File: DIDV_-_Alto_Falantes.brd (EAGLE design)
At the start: 74.9 x 59.4 mm, 41 parts, among them J101 PG203J, J102 PG203J, U101 LM386M, U102 LM386M

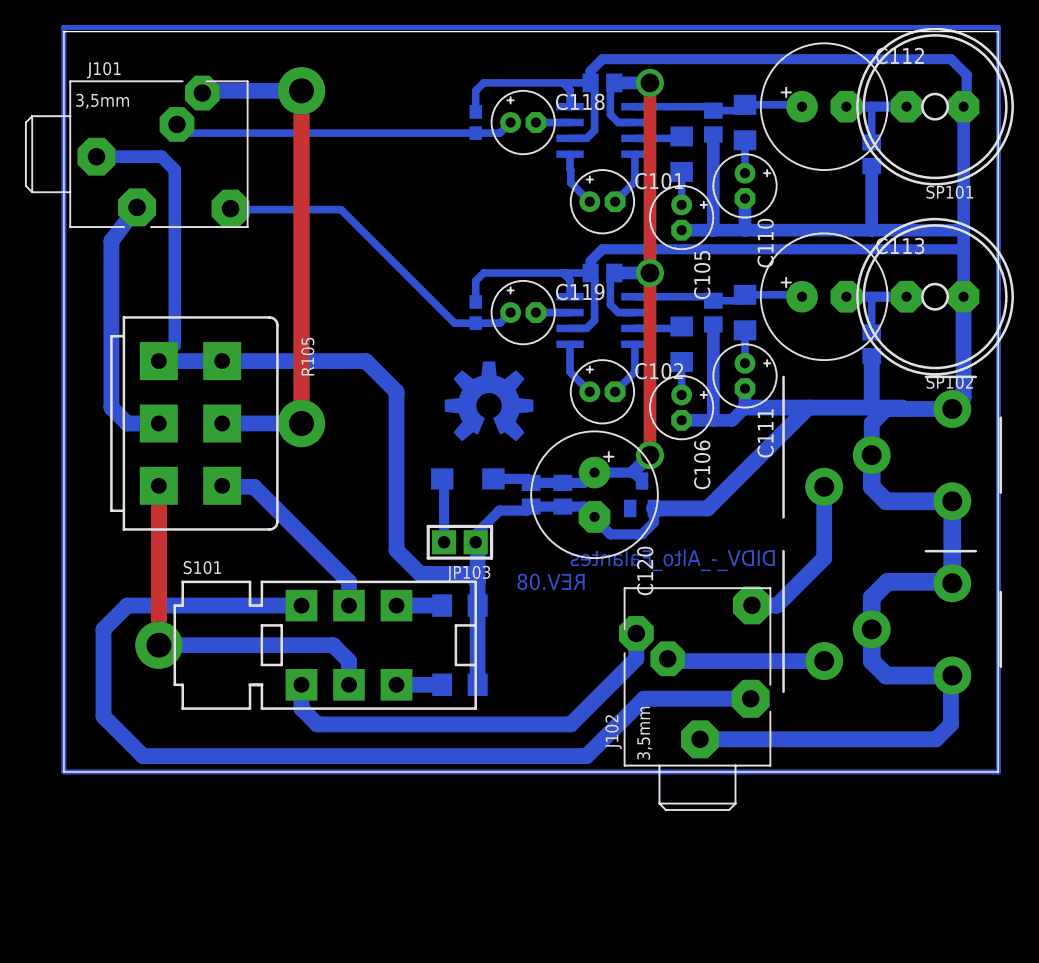
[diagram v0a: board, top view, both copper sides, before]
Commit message: Revisão 9
- Corrigidos algumas falhas de ligação
- Implementação com VPRG dos TLCs via Hardware
- Inserção do cálculo do Riref

Obs. Se somente a criação de boards, não será incrementado. No caso, se criado um board novo board vou subir para 9.1 e assim por diante.
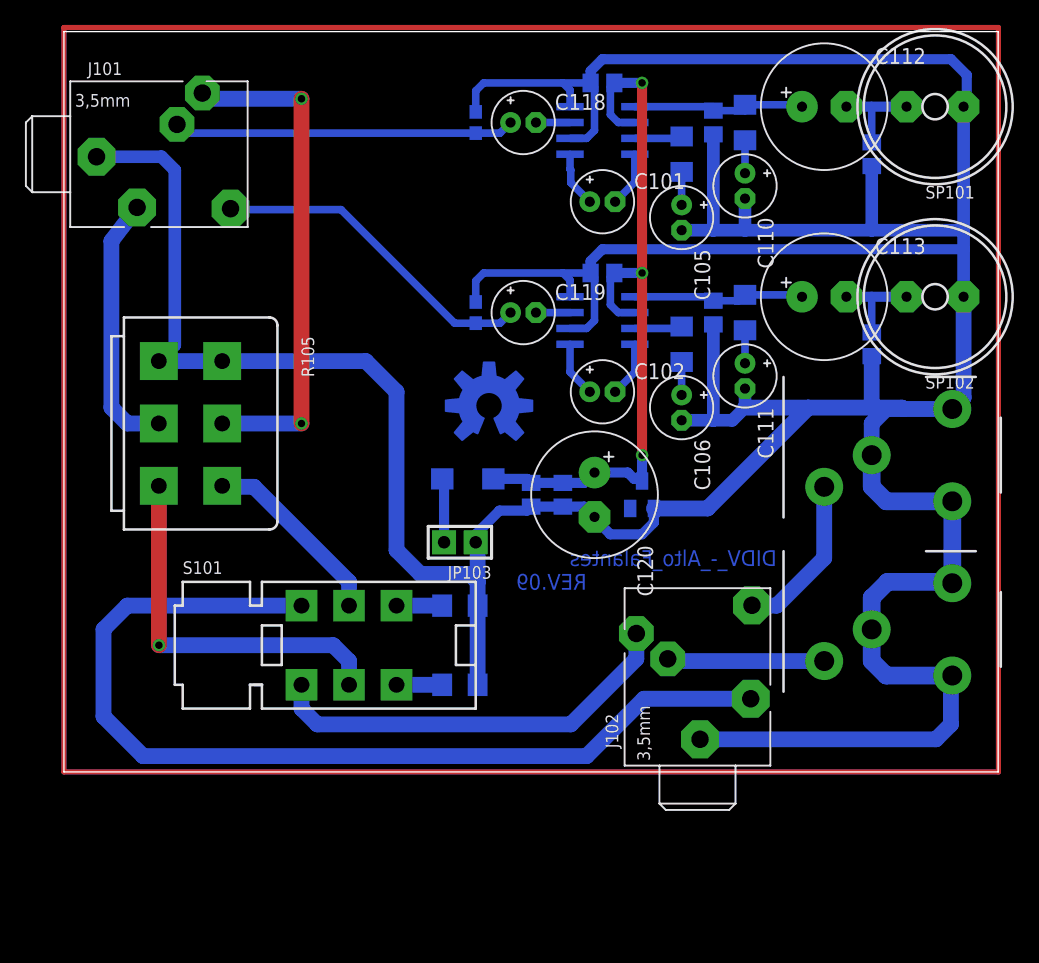
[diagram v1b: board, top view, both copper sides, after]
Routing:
- net N$20: track 0.00 -> 269.2 mm
- net VCC: track 60.0 -> 58.8 mm
- net A_R: track 41.9 -> 41.0 mm
- added copper zone on layer 1, net N$22
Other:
- board text added: "REV.09"
- board text removed: "REV.08"

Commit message: Revisão 10
Revisão representa o estado final do projeto, alterações agora somente referentes a valores de componentes e adaptações se e somente se não existir a possibilidade de manobras via software.

Placas nas dimensões e condições as quais foram submetidas a cotação para confecção em local especializado.
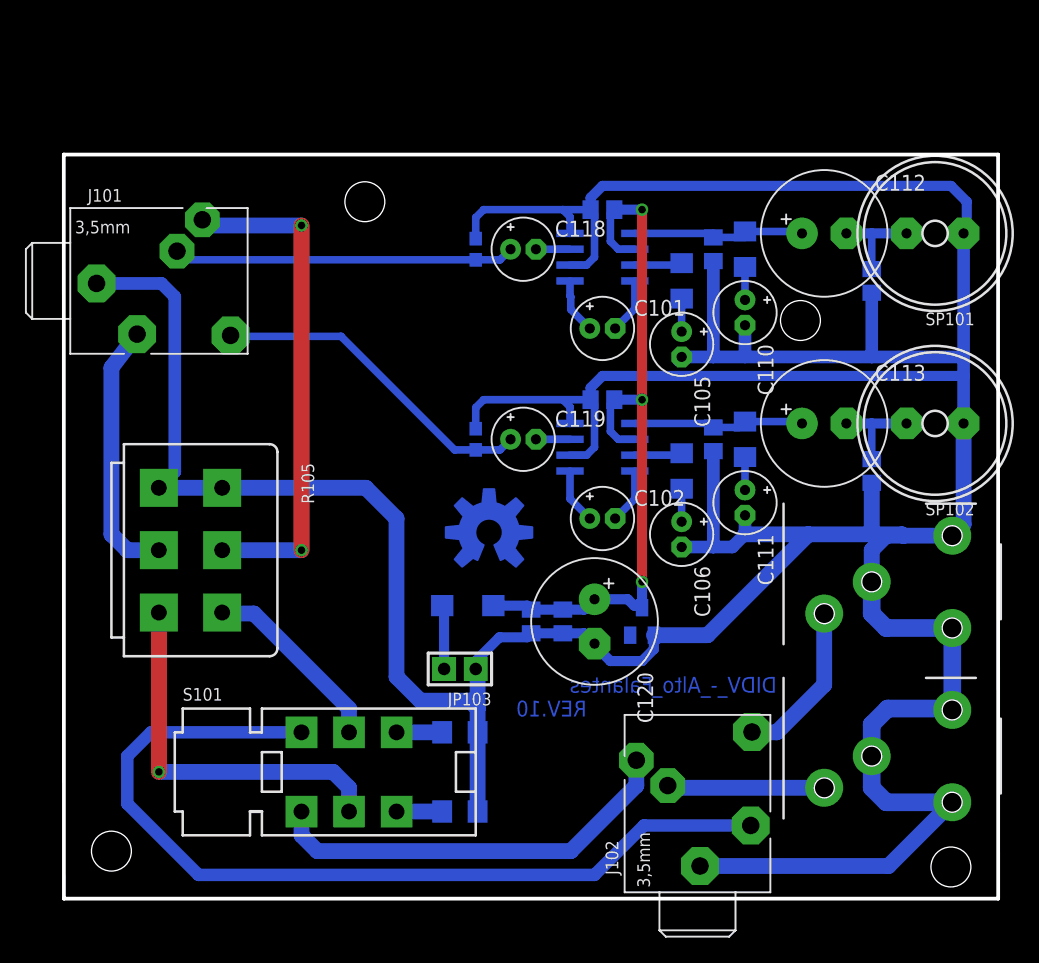
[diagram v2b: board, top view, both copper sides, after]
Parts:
- moved C101 10.2 mm to (43.2, 45.7)
- moved C104 10.2 mm to (43.2, 55.2)
- moved C109 10.2 mm to (52.1, 36.8)
- moved C115 10.2 mm to (64.8, 34.3)
- moved C117 10.2 mm to (33.0, 36.8)
- moved C119 10.2 mm to (36.8, 36.8)
- moved JP101 10.2 mm to (71.1, 25.4)
- moved R102 10.2 mm to (49.5, 34.3)
- moved R104 10.2 mm to (54.6, 36.8)
- moved C102 10.2 mm to (43.2, 30.5)
- moved D101 10.2 mm to (32.4, 23.5)
- moved J102 10.2 mm to (50.8, 7.62)
- moved JP102 10.2 mm to (71.1, 11.4)
- moved JP103 10.2 mm to (31.8, 18.4)
- moved R105 10.2 mm to (3.81, 27.9)
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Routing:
- net N$20: track 269.2 -> 0.00 mm
- net N$19: track 269.2 -> 0.00 mm
- net AUDIO_R: track 78.8 -> 72.6 mm
- net GND: track 378.4 -> 376.3 mm
- added copper zone on layer 1, net GND
- removed copper zone on layer 1, net N$22
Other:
- board size 74.9 x 59.4 mm -> 74.9 x 59.7 mm
- board text added: "REV.10"
- board text removed: "REV.09"
